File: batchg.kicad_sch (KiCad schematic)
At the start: 38 parts, among them J10 CELLS1, J14 Barrel_Jack, J7 Conn_01x03, J8 Conn_01x03, J9 CELLS1, Q8 IRLZ44NSTRL(UMW), Q9 IRLZ44NSTRL(UMW), U7 LTC4162EUFD

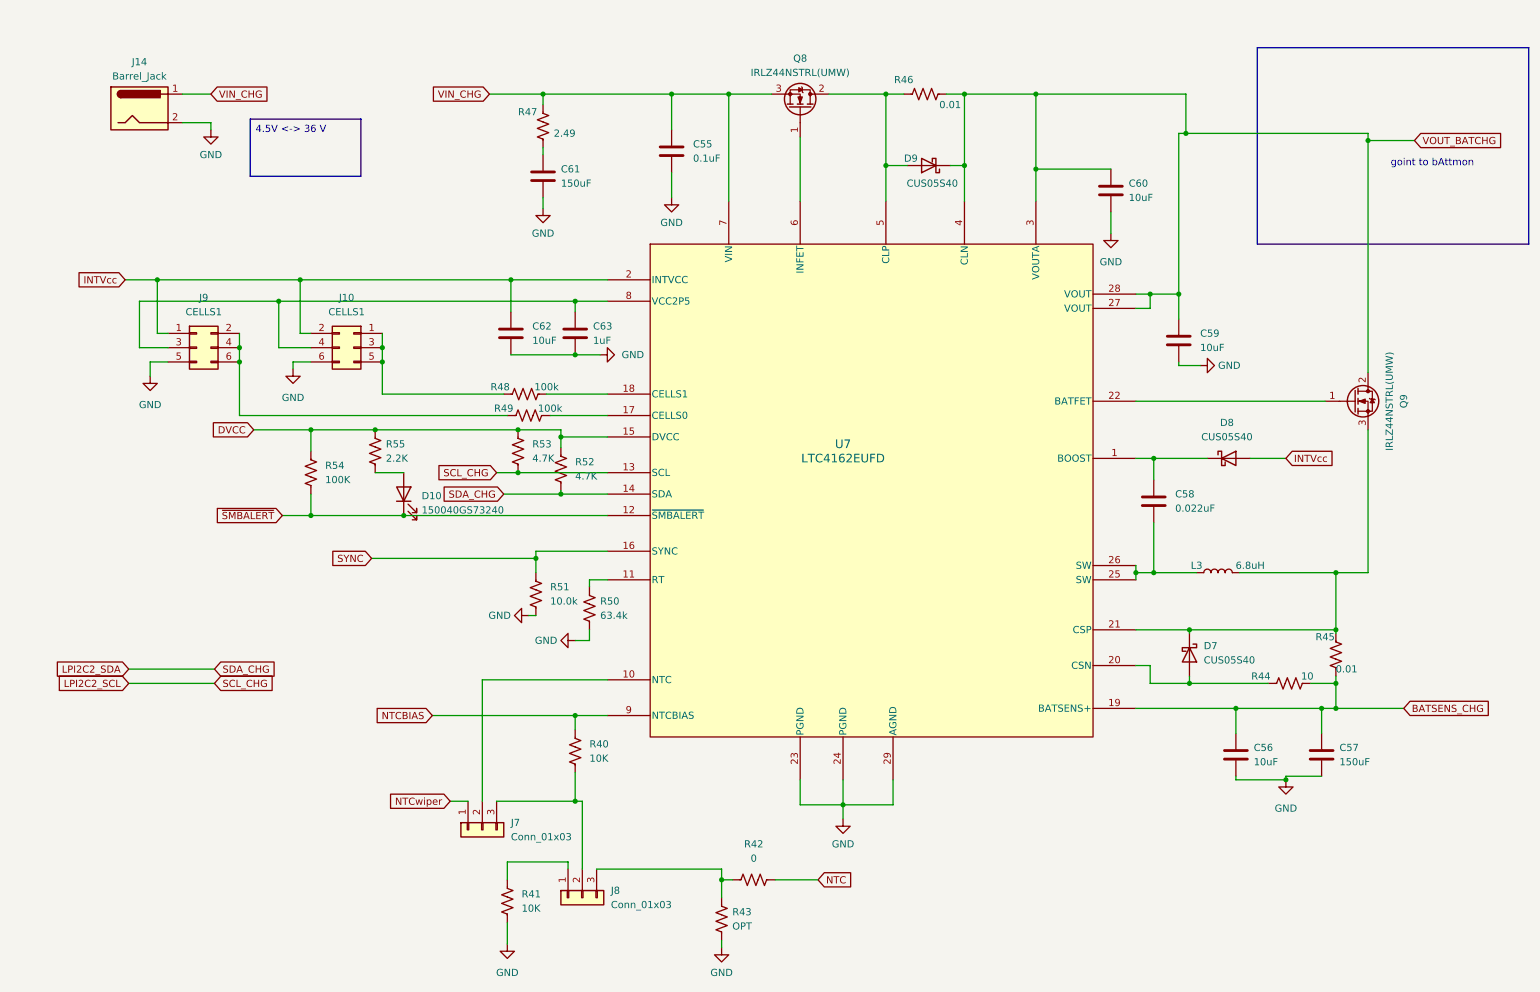
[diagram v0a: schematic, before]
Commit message: add revision to motor
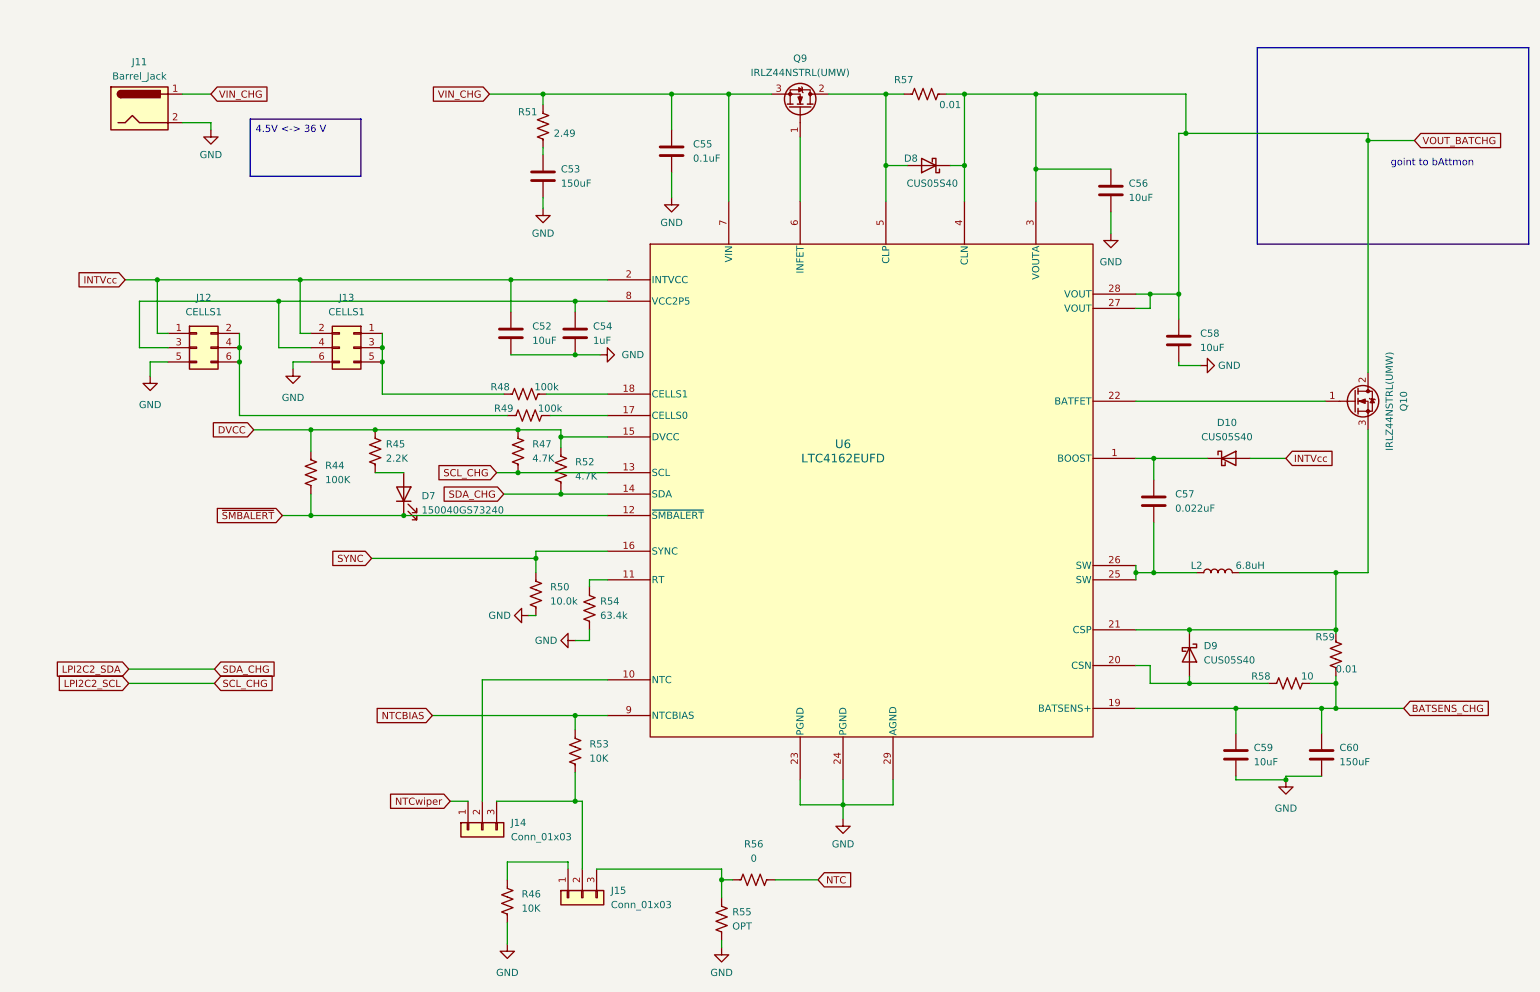
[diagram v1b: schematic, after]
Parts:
- C53: renamed from C61; footprint Capacitor_SMD:C_0603_1608Metric -> Capacitor_SMD:CP_Elec_10x10.5
- C60: renamed from C57; footprint Capacitor_SMD:C_0603_1608Metric -> Capacitor_SMD:CP_Elec_10x10.5; JLCPARTS (none) -> EEEFK1H151P; Manufacture (none) -> EEEFK1H151P; Manufacturer_Part_Number (none) -> EEEFK1H151P
- L2: renamed from L3; footprint Inductor_SMD:L_APV_APH0620 -> Inductor_SMD:L_Murata_DFE201610P; PartNum CXP0620-6R8M-AG(6.8uh) -> MAI201610S-6R8MT
- renumbered C62 to C52, C63 to C54, C60 to C56, C58 to C57, C59 to C58, C56 to C59, D8 to D10, D10 to D7, D9 to D8, D7 to D9, J14 to J11, J9 to J12, J10 to J13, J7 to J14, J8 to J15, Q9 to Q10, Q8 to Q9, R54 to R44, R55 to R45, R41 to R46, R53 to R47, R51 to R50, R47 to R51, R40 to R53, R50 to R54, R43 to R55, R42 to R56, R46 to R57, R44 to R58, R45 to R59, U7 to U6

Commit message: del some
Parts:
- renumbered J11 to J12, J12 to J13, J13 to J14, J14 to J15, J15 to J16
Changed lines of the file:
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@@
 		(on_board yes)
 		(dnp no)
-		(property "Reference" "J13"
+		(property "Reference" "J14"
 			(at 71.12 69.85 0)
 			(effects
@@
 			(project "qiot"
 				(path "/0db193be-516d-4409-bb62-b8733a9e8874/b821f11b-e956-4fb1-8b7f-25db230f4b78"
-					(reference "J13")
+					(reference "J14")
 					(unit 1)
 				)
@@
 		(dnp no)
 		(fields_autoplaced yes)
-		(property "Reference" "J15"
+		(property "Reference" "J16"
 			(at 118.11 175.2599 90)
 			(effects
@@
 			(project "qiot"
 				(path "/0db193be-516d-4409-bb62-b8733a9e8874/b821f11b-e956-4fb1-8b7f-25db230f4b78"
-					(reference "J15")
+					(reference "J16")
 					(unit 1)
 				)
@@
 		(dnp no)
 		(fields_autoplaced yes)
-		(property "Reference" "J11"
+		(property "Reference" "J12"
 			(at 34.29 27.94 0)
 			(effects
@@
 			(project "qiot"
 				(path "/0db193be-516d-4409-bb62-b8733a9e8874/b821f11b-e956-4fb1-8b7f-25db230f4b78"
-					(reference "J11")
+					(reference "J12")
 					(unit 1)
 				)
@@
 		(dnp no)
 		(fields_autoplaced yes)
-		(property "Reference" "J12"
+		(property "Reference" "J13"
 			(at 45.72 69.85 0)
 			(effects
@@
 			(project ""
 				(path "/0db193be-516d-4409-bb62-b8733a9e8874/b821f11b-e956-4fb1-8b7f-25db230f4b78"
-					(reference "J12")
+					(reference "J13")
 					(unit 1)
 				)
@@
 		(dnp no)
 		(fields_autoplaced yes)
-		(property "Reference" "J14"
+		(property "Reference" "J15"
 			(at 100.33 163.1949 90)
 			(effects
@@
 			(project ""
 				(path "/0db193be-516d-4409-bb62-b8733a9e8874/b821f11b-e956-4fb1-8b7f-25db230f4b78"
-					(reference "J14")
+					(reference "J15")
 					(unit 1)
 				)

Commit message: dad
da
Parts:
- C52, C56, C58, C59: Manufacturer_Part_Number (none) -> CS1608X5R106M160NRB
- C53: Manufacturer_Part_Number (none) -> EEEFK1H151P
- C54: Manufacturer_Part_Number (none) -> CL05A105KO5NNNC
- C55: value 0.1uF -> 100nF; Manufacturer_Part_Number (none) -> CS1005X7R104K500NR
- C57: value 0.022uF -> 22nF; Manufacturer_Part_Number (none) -> GRM155R71H223KA12D
- D10, D8, D9: Manufacturer_Part_Number (none) -> CUS05S40.H3F
- D7: Manufacturer_Part_Number (none) -> C6210741
- J12, J13, J14, J15, J16, R55: now not fitted
- L2: Manufacturer_Part_Number (none) -> YSMC201610H-6R8MB
- Q10, Q9: Manufacturer_Part_Number (none) -> IRLZ44NSTRL(UMW)
- R44: Manufacturer_Part_Number (none) -> RC0402FR-07100KL
- R45: Manufacturer_Part_Number (none) -> RC0402FR-072K2L
- R46, R53: Manufacturer_Part_Number (none) -> RC0402FR-0710KL
- R47, R52: Manufacturer_Part_Number (none) -> RC0402FR-074K7L
- R48, R49: value 100k -> 100K; Manufacturer_Part_Number (none) -> RC0402FR-07100KL
- R50: value 10.0k -> 10K; Manufacturer_Part_Number (none) -> RC0402FR-0710KL
- R51: Manufacturer_Part_Number (none) -> CRCW04022R49FKED
- R54: value 63.4k -> 63.4K; Manufacturer_Part_Number (none) -> FRC0402F6342TS
- R56: Manufacturer_Part_Number (none) -> RC0402FR-070RL
- R57, R59: Manufacturer_Part_Number (none) -> RC0402FR-0710ML
- R58: Manufacturer_Part_Number (none) -> FRC0402F10R0TS
- U6: Manufacturer_Part_Number (none) -> LTC4162EUFD

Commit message: gema
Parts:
- removed J12: Barrel_Jack, Connector_BarrelJack:BarrelJack_Horizontal, symbol Connector:Barrel_Jack
- added J4: PJ-102AH, footprints:DC-IN-TH_PJ-102AH, symbol Connector:Barrel_Jack_Switch_Pin3Ring
- C52, C56, C58, C59:  LCSC Part # (none) -> C194427; Manufacturer_Part_Number CS1608X5R106M160NRB -> GRM188R6YA106MA73D
- C53, C60:  LCSC Part # (none) -> C413508
- C54:  LCSC Part # (none) -> C29266
- C55:  LCSC Part # (none) -> C77020; Manufacturer_Part_Number CS1005X7R104K500NR -> GRM155R71H104KE14D
- C57:  LCSC Part # (none) -> C77023
- D10, D8, D9:  LCSC Part # (none) -> C2762696
- D7:  LCSC Part # (none) -> C6210741
- L2:  LCSC Part # (none) -> C41405888
- Q10, Q9:  LCSC Part # (none) -> C42370422
- R44, R48, R49:  LCSC Part # (none) -> C60491
- R45:  LCSC Part # (none) -> C114762
- R46, R50, R53:  LCSC Part # (none) -> C60490
- R47, R52:  LCSC Part # (none) -> C105871
- R51:  LCSC Part # (none) -> C2085509
- R54:  LCSC Part # (none) -> C2933107
- R56:  LCSC Part # (none) -> C106231
- R57, R59:  LCSC Part # (none) -> C138067
- R58:  LCSC Part # (none) -> C2906862
- U6:  LCSC Part # (none) -> C3681528
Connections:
- net GND: now also J4.3
- net VIN_CHG: now also J4.1
